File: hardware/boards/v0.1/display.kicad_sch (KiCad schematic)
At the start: 13 parts, among them U26 ER-TFT028A-4, U27 TPS92360, U37 ER-TPC028-4.1

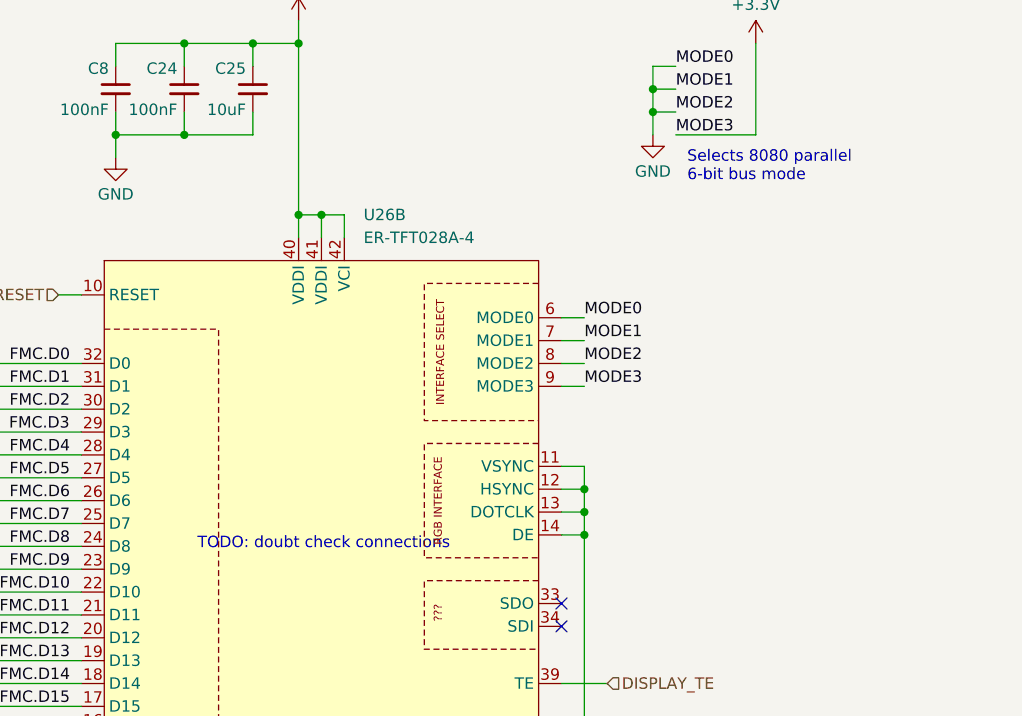
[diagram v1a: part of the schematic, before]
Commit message: feat: various layout and routing adjustments
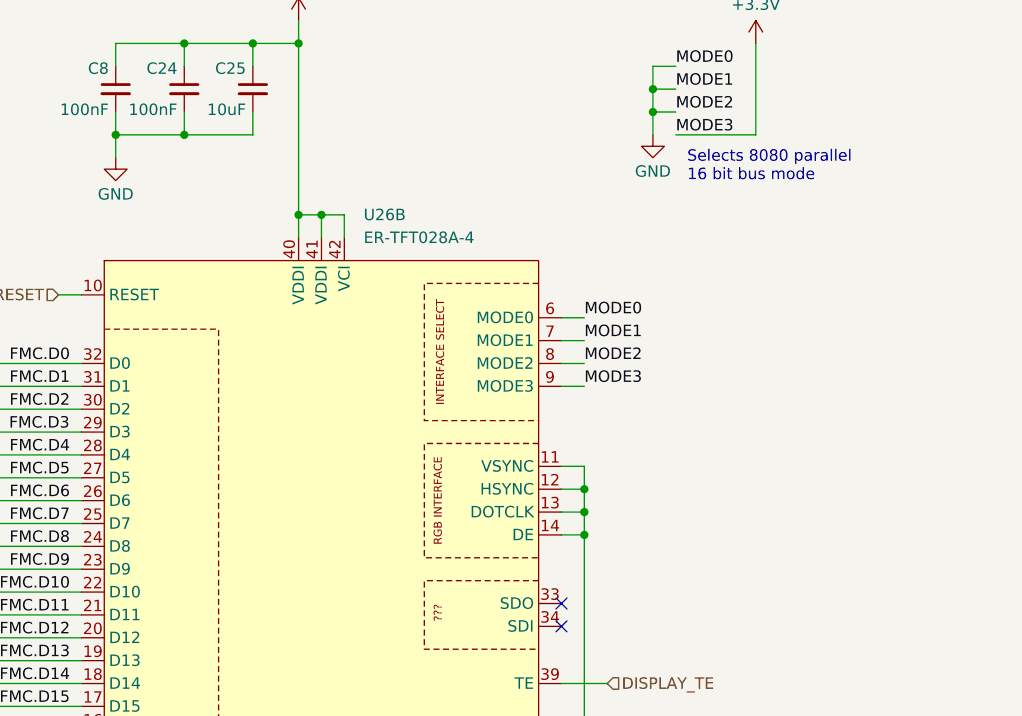
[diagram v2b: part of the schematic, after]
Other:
- note added: "Selects 8080 parallel 16 bit bus mode"
- note removed: "Selects 8080 parallel 6-bit bus mode"
- note removed: "TODO: doubt check connections"
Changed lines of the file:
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@@
 		)
 	)
-	(text "Selects 8080 parallel\n6-bit bus mode"
+	(text "Selects 8080 parallel\n16 bit bus mode"
 		(exclude_from_sim no)
 		(at 106.68 41.656 0)
@@
 		)
 	)
-	(text "TODO: doubt check connections"
-		(exclude_from_sim no)
-		(at 66.294 83.566 0)
-		(effects
-			(font
-				(size 1.27 1.27)
-			)
-		)
-	)
 	(junction
 		(at 92.71 148.59)
@@
 			)
 		)
-		(property "Characteristics " ""
-			(at 63.5 153.67 0)
-			(effects
-				(font
-					(size 1.27 1.27)
-				)
-			)
-		)
 		(property "Sim.Enable" ""
 			(at 63.5 153.67 0)
@@
 			)
 		)
-		(property "Characteristics " ""
-			(at 81.28 161.29 0)
-			(effects
-				(font
-					(size 1.27 1.27)
-				)
-			)
-		)
 		(property "Sim.Enable" ""
 			(at 81.28 161.29 0)
@@
 			)
 		)
-		(property "Characteristics " ""
-			(at 179.07 82.55 0)
-			(effects
-				(font
-					(size 1.27 1.27)
-				)
-			)
-		)
 		(property "Sim.Enable" ""
 			(at 179.07 82.55 0)
@@
 			)
 		)
-		(property "Characteristics " ""
-			(at 105.41 153.67 0)
-			(effects
-				(font
-					(size 1.27 1.27)
-				)
-			)
-		)
 		(property "Sim.Enable" ""
 			(at 105.41 153.67 0)
@@
 			)
 		)
-		(property "Characteristics " ""
-			(at 58.42 33.02 0)
-			(effects
-				(font
-					(size 1.27 1.27)
-				)
-			)
-		)
 		(property "Sim.Enable" ""
 			(at 58.42 33.02 0)
@@
 			)
 		)
-		(property "Characteristics " ""
-			(at 99.06 148.59 0)
-			(effects
-				(font
-					(size 1.27 1.27)
-				)
-			)
-		)
 		(property "Sim.Enable" ""
 			(at 99.06 148.59 0)
@@
 	)
 	(symbol
-		(lib_name "ER-TFT028A2-4_1")
 		(lib_id "pocket_synth:ER-TFT028A2-4")
 		(at 207.01 137.16 0)
@@
 			)
 		)
-		(property "Characteristics " ""
-			(at 207.01 137.16 0)
-			(effects
-				(font
-					(size 1.27 1.27)
-				)
-			)
-		)
 		(property "Sim.Enable" ""
 			(at 207.01 137.16 0)
@@
 	)
 	(symbol
-		(lib_name "ER-TFT028A2-4_2")
 		(lib_id "pocket_synth:ER-TFT028A2-4")
 		(at 66.04 88.9 0)
@@
 			)
 		)
-		(property "Characteristics " ""
-			(at 66.04 88.9 0)
-			(effects
-				(font
-					(size 1.27 1.27)
-				)
-			)
-		)
 		(property "Sim.Enable" ""
 			(at 66.04 88.9 0)
@@
 			)
 		)
-		(property "Characteristics " ""
-			(at 123.19 156.21 0)
-			(effects
-				(font
-					(size 1.27 1.27)
-				)
-			)
-		)
 		(property "Sim.Enable" ""
 			(at 123.19 156.21 0)
@@
 			)
 		)
-		(property "Characteristics " ""
-			(at 68.58 168.91 0)
-			(effects
-				(font
-					(size 1.27 1.27)
-				)
-			)
-		)
 		(property "Sim.Enable" ""
 			(at 68.58 168.91 0)
@@
 			)
 		)
-		(property "Characteristics " ""
-			(at 50.8 33.02 0)
-			(effects
-				(font
-					(size 1.27 1.27)
-				)
-			)
-		)
 		(property "Sim.Enable" ""
 			(at 50.8 33.02 0)
@@
 			)
 		)
-		(property "Characteristics " ""
-			(at 81.28 148.59 0)
-			(effects
-				(font
-					(size 1.27 1.27)
-				)
-			)
-		)
 		(property "Sim.Enable" ""
 			(at 81.28 148.59 0)
@@
 			)
 		)
-		(property "Characteristics " ""
-			(at 93.98 172.72 0)
-			(effects
-				(font
-					(size 1.27 1.27)
-				)
-			)
-		)
 		(property "Sim.Enable" ""
 			(at 93.98 172.72 0)
@@
 			)
 		)
-		(property "Characteristics " ""
-			(at 43.18 33.02 0)
-			(effects
-				(font
-					(size 1.27 1.27)
-				)
-			)
-		)
 		(property "Sim.Enable" ""
 			(at 43.18 33.02 0)
@@
 			)
 		)
-		(property "Characteristics " ""
-			(at 222.25 81.28 0)
-			(effects
-				(font
-					(size 1.27 1.27)
-				)
-			)
-		)

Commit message: chore: final DFM modifications?
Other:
- moved on the sheet: C107, C80, D17, L5, R11, R52, TP47, U26A, U26C, U27, U37
